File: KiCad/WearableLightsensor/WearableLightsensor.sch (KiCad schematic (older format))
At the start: 2 parts

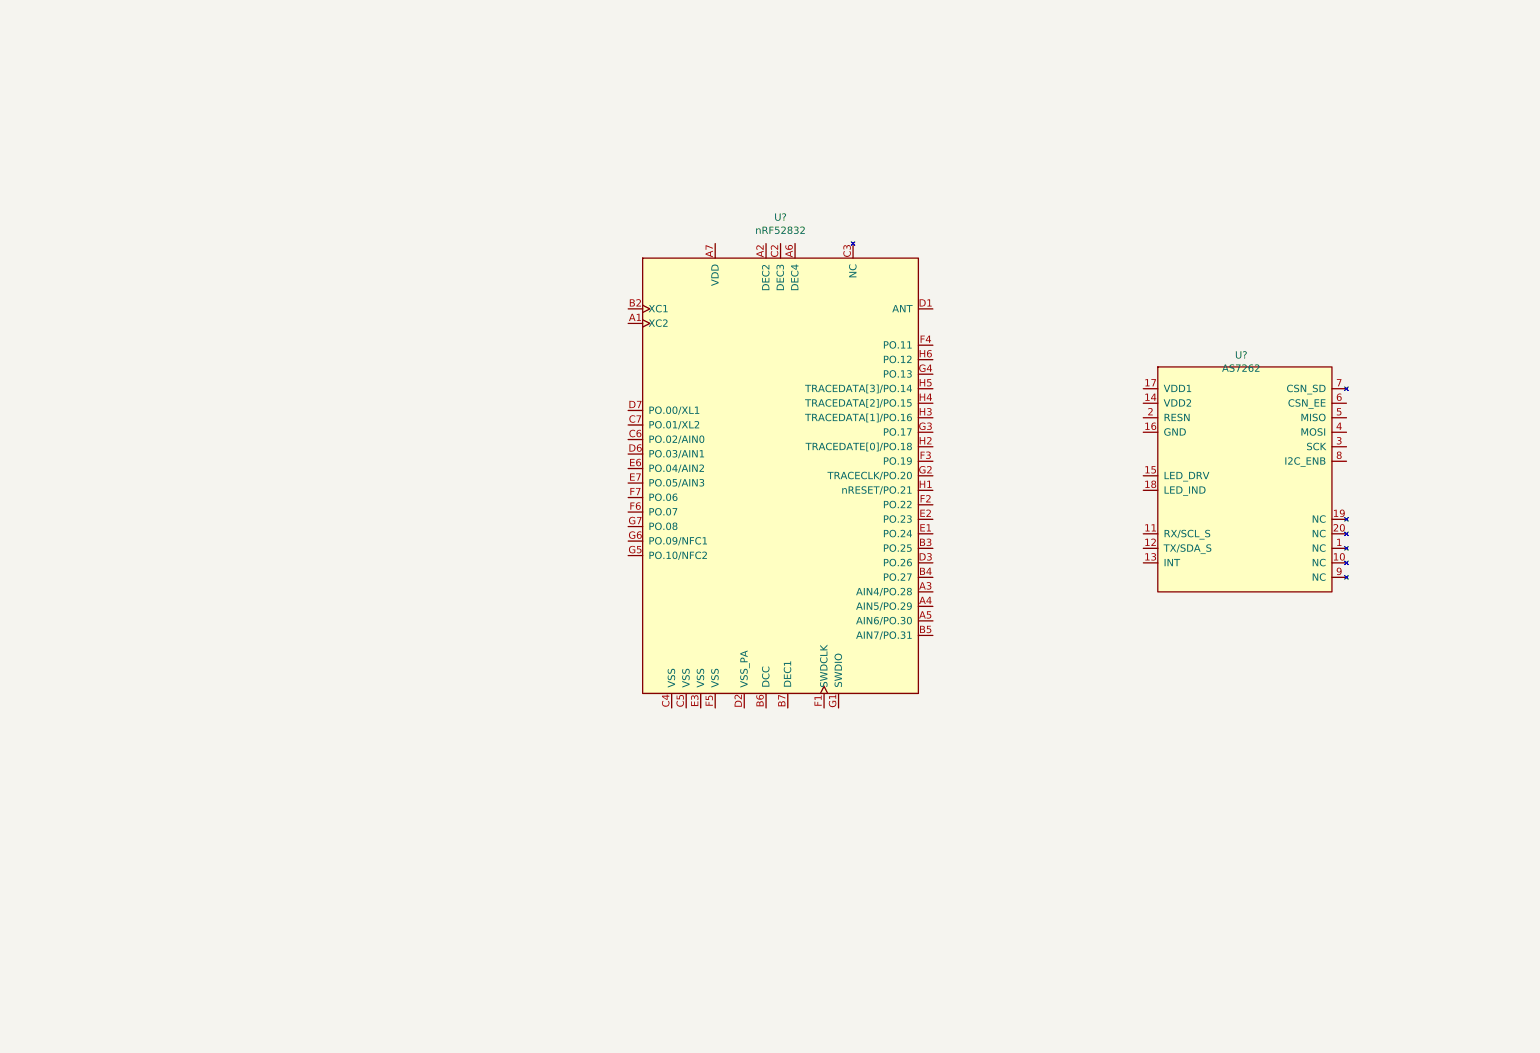
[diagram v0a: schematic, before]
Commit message: Finalize schematic. Begin work on layout
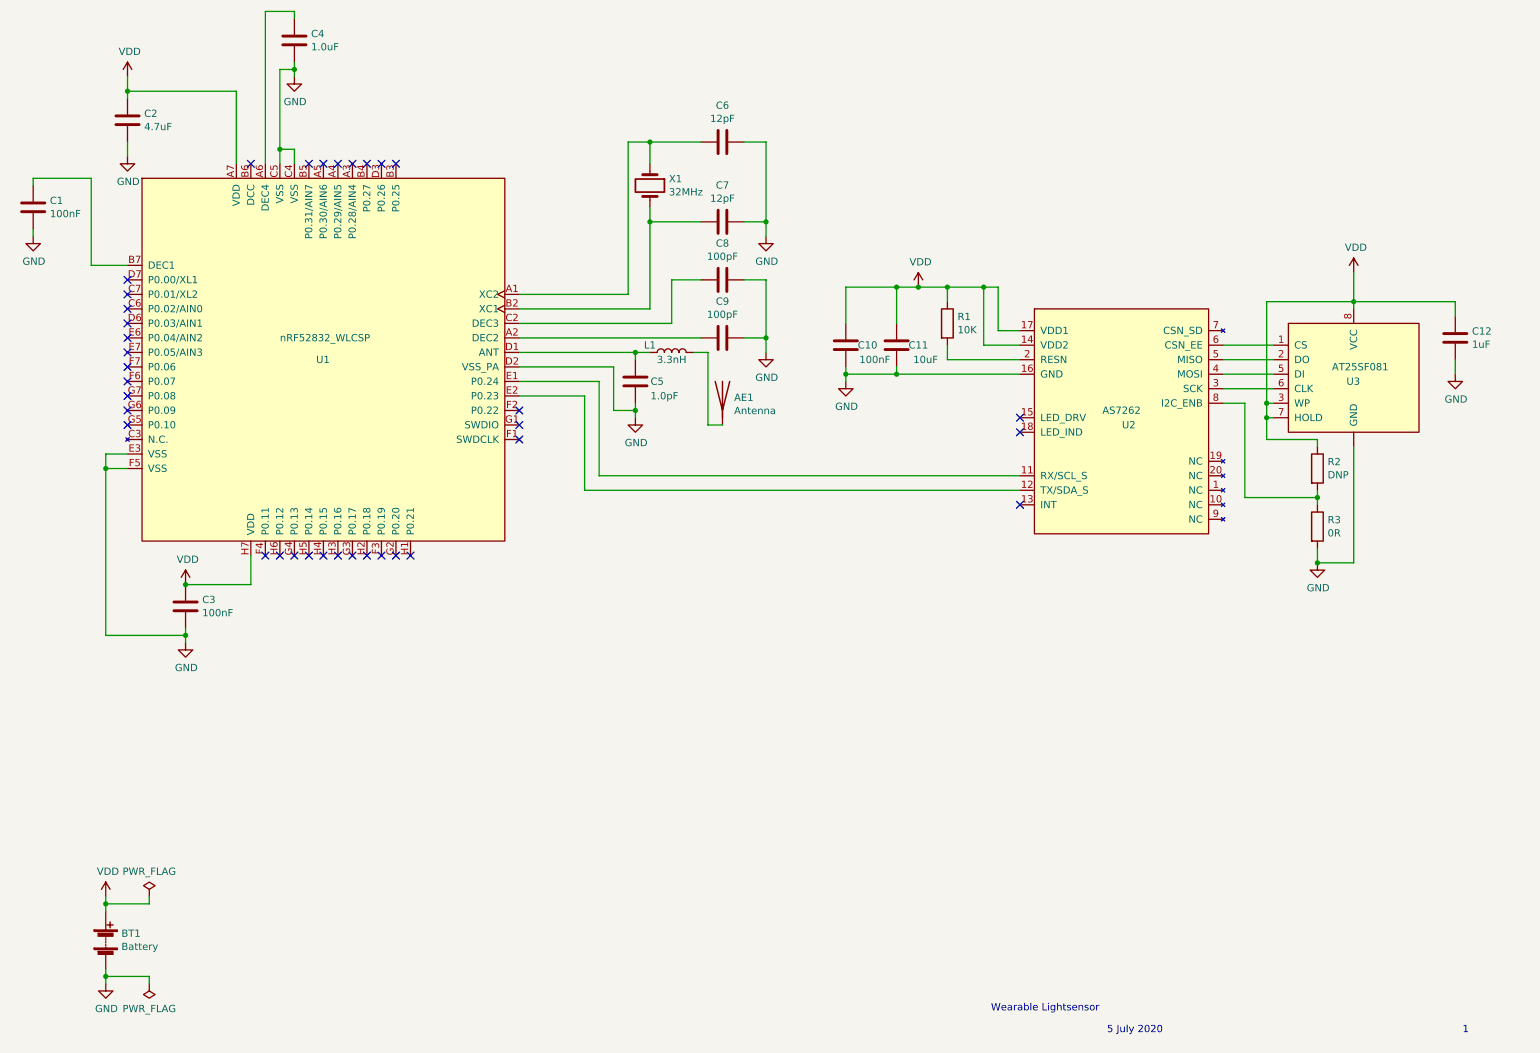
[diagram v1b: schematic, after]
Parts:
- removed U?: nRF52832, symbol WearableLightsensor:nRF52832
- removed U?: AS7262, symbol WearableLightsensor:AS7262
- added AE1: Antenna, RF_Antenna:Texas_SWRA117D_2.4GHz_Left, symbol Device:Antenna
- added BT1: Battery, Battery:BatteryHolder_MPD_BC2003_1x2032, symbol Device:Battery
- added C1, C10, C3: 100nF, Capacitor_SMD:C_0201_0603Metric, symbol Device:C
- added C11: 10uF, Capacitor_SMD:C_0603_1608Metric, symbol Device:C
- added C12: 1uF, Capacitor_SMD:C_0402_1005Metric, symbol Device:C
- added C2: 4.7uF, Capacitor_SMD:C_0603_1608Metric, symbol Device:C
- added C4: 1.0uF, Capacitor_SMD:C_0402_1005Metric, symbol Device:C
- added C5: 1.0pF, Capacitor_SMD:C_0201_0603Metric, symbol Device:C
- added C6, C7: 12pF, Capacitor_SMD:C_0201_0603Metric, symbol Device:C
- added C8, C9: 100pF, Capacitor_SMD:C_0201_0603Metric, symbol Device:C
- added L1: 3.3nH, Inductor_SMD:L_0201_0603Metric, symbol Device:L
- added R1: 10K, Capacitor_SMD:C_0402_1005Metric, symbol Device:R
- added R2: DNP, Capacitor_SMD:C_0402_1005Metric, symbol Device:R
- added R3: 0R, Capacitor_SMD:C_0402_1005Metric, symbol Device:R
- added U1: nRF52832_WLCSP, FootprintLib:BGA-56_7x8_2.956x3.226mm, symbol WearableLightsensor:nRF52832_WLCSP
- added U2: AS7262, Package_LGA:AMS_LGA-20_4.7x4.5mm_P0.65mm, symbol WearableLightsensor:AS7262
- added U3: AT25SF081, Package_SO:SOIC-8_3.9x4.9mm_P1.27mm, symbol WearableLightsensor:AT25SF081
- added X1: 32MHz, Crystal:Crystal_SMD_2016-4Pin_2.0x1.6mm, symbol Device:Crystal
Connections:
- new net: C6.2, U1.A1 (XC2), X1.1
- new net: C9.2, U1.A2 (DEC2)
- new net: C4.1, U1.A6 (DEC4)
- new net: C7.2, U1.B2 (XC1), X1.2
- new net: C1.1, U1.B7 (DEC1)
- new net: C8.2, U1.C2 (DEC3)
- new net: C5.2, L1.1, U1.D1 (ANT)
- new net: U1.E1 (P0.24), U2.11 (RX/SCL_S)
- new net: U1.E2 (P0.23), U2.12 (TX/SDA_S)
- new net: AE1.1 (A), L1.2
- new net: R1.2, U2.2 (RESN)
- new net: U2.3 (SCK), U3.6 (CLK)
- new net: U2.4 (MOSI), U3.5 (DI)
- new net: U2.5 (MISO), U3.2 (DO)
- new net: U2.6 (CSN_EE), U3.1 (CS)
- new net: R2.2, R3.1, U2.8 (I2C_ENB)
- new net GND: BT1.2 (-), C1.2, C10.1, C11.1, C12.2, C2.2, C3.2, C4.2, C5.1, C6.1, C7.1, C8.1, C9.1, R3.2, U1.C4 (VSS), U1.C5 (VSS), U1.D2 (VSS_PA), U1.E3 (VSS), U1.F5 (VSS), U2.16 (GND), U3.~ (GND)
- new net VDD: BT1.1 (+), C10.2, C11.2, C12.1, C2.1, C3.1, R1.1, R2.1, U1.A7 (VDD), U1.H7 (VDD), U2.14 (VDD2), U2.17 (VDD1), U3.3 (WP), U3.7 (HOLD), U3.8 (VCC)
- no-connect marks 0 -> 36
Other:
- note added: "1"
- note added: "5 July 2020"
- note added: "Wearable Lightsensor"

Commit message: Revert to QFN package. There is enough room
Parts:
- removed AE1: Antenna, RF_Antenna:Texas_SWRA117D_2.4GHz_Left, symbol Device:Antenna
- removed C1, C3: 100nF, Capacitor_SMD:C_0201_0603Metric, symbol Device:C
- removed C2: 4.7uF, Capacitor_SMD:C_0603_1608Metric, symbol Device:C
- removed C4: 1.0uF, Capacitor_SMD:C_0402_1005Metric, symbol Device:C
- removed C5: 1.0pF, Capacitor_SMD:C_0201_0603Metric, symbol Device:C
- removed C6, C7: 12pF, Capacitor_SMD:C_0201_0603Metric, symbol Device:C
- removed C8, C9: 100pF, Capacitor_SMD:C_0201_0603Metric, symbol Device:C
- removed L1: 3.3nH, Inductor_SMD:L_0201_0603Metric, symbol Device:L
- removed U1: nRF52832_WLCSP, FootprintLib:BGA-56_7x8_2.956x3.226mm, symbol WearableLightsensor:nRF52832_WLCSP
- removed X1: 32MHz, Crystal:Crystal_SMD_2016-4Pin_2.0x1.6mm, symbol Device:Crystal
- added AE?: Antenna, RF_Antenna:Texas_SWRA117D_2.4GHz_Left, symbol Device:Antenna
- added C? (x2): 12pF, Capacitor_SMD:C_0402_1005Metric, symbol Device:C
- added C?: 100pF, Capacitor_SMD:C_0402_1005Metric, symbol Device:C
- added C?: N.C., Capacitor_SMD:C_0402_1005Metric, symbol Device:C
- added C?: 0.8pF, Capacitor_SMD:C_0402_1005Metric, symbol Device:C
- added C? (x3): 100nF, Capacitor_SMD:C_0402_1005Metric, symbol Device:C
- added C?: 4.7uF, Capacitor_SMD:C_0603_1608Metric, symbol Device:C
- added C?: 1.0uF, Capacitor_SMD:C_0603_1608Metric, symbol Device:C
- added L?: 3.9nH, Inductor_SMD:L_0402_1005Metric, symbol Device:L
- added U?: nRF52832_QFN, symbol WearableLightsensor:nRF52832_QFN
- added X?: 32MHz, Crystal:Crystal_SMD_2016-4Pin_2.0x1.6mm, symbol Device:Crystal
- U3: symbol WearableLightsensor:AT25SF081 -> WearableLightsensor-rescue:AT25SF081-WearableLightsensor
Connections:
- net labels added: SCL, SDA
- no-connect marks 36 -> 3
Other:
- note added: "MICROCONTROLLER"
- note added: "POWER\n"
- note added: "SENSOR"
- moved on the sheet: BT1, C10, C11, C12, R1, R2, R3, U2

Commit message: Fix uP symbol and make schematic pass ERC
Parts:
- U1: renamed from U?; footprint (none) -> Package_DFN_QFN:QFN-48-1EP_6x6mm_P0.4mm_EP4.6x4.6mm
- gave numbers to parts that had none: 13
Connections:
- no-connect marks 3 -> 37
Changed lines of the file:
@@
 5 July 2020
 $Comp
-L WearableLightsensor:nRF52832_QFN U?
+L WearableLightsensor:nRF52832_QFN U1
 U 1 1 5F301DDC
 P 2750 5800
-F 0 "U?" H 2750 5900 50  0000 L CNN
+F 0 "U1" H 2750 5900 50  0000 L CNN
 F 1 "nRF52832_QFN" H 2500 6000 50  0000 L CNN
-F 2 "" H 2750 5800 50  0001 C CNN
+F 2 "Package_DFN_QFN:QFN-48-1EP_6x6mm_P0.4mm_EP4.6x4.6mm" H 2750 5800 50  0001 C CNN
 F 3 "" H 2750 5800 50  0001 C CNN
 	1    2750 5800
@@
 $EndComp
 $Comp
-L Device:Crystal X?
+L Device:Crystal X1
 U 1 1 5F311D90
 P 4900 4000
-F 0 "X?" V 4854 4131 50  0000 L CNN
+F 0 "X1" V 4854 4131 50  0000 L CNN
 F 1 "32MHz" V 4945 4131 50  0000 L CNN
 F 2 "Crystal:Crystal_SMD_2016-4Pin_2.0x1.6mm" H 4900 4000 50  0001 C CNN
@@
 $EndComp
 $Comp
-L Device:C C?
+L Device:C C8
 U 1 1 5F313B1A
 P 5400 4200
-F 0 "C?" V 5148 4200 50  0000 C CNN
+F 0 "C8" V 5148 4200 50  0000 C CNN
 F 1 "12pF" V 5239 4200 50  0000 C CNN
 F 2 "Capacitor_SMD:C_0402_1005Metric" H 5438 4050 50  0001 C CNN
@@
 $EndComp
 $Comp
-L Device:C C?
+L Device:C C7
 U 1 1 5F314DA8
 P 5400 3800
-F 0 "C?" V 5148 3800 50  0000 C CNN
+F 0 "C7" V 5148 3800 50  0000 C CNN
 F 1 "12pF" V 5239 3800 50  0000 C CNN
 F 2 "Capacitor_SMD:C_0402_1005Metric" H 5438 3650 50  0001 C CNN
@@
 $EndComp
 $Comp
-L power:GND #PWR?
+L power:GND #PWR017
 U 1 1 5F31610B
 P 5700 4400
-F 0 "#PWR?" H 5700 4150 50  0001 C CNN
+F 0 "#PWR017" H 5700 4150 50  0001 C CNN
 F 1 "GND" H 5705 4227 50  0000 C CNN
 F 2 "" H 5700 4400 50  0001 C CNN
@@
 Connection ~ 4900 4200
 $Comp
-L Device:C C?
+L Device:C C9
 U 1 1 5F320F0A
 P 5400 4700
-F 0 "C?" V 5148 4700 50  0000 C CNN
+F 0 "C9" V 5148 4700 50  0000 C CNN
 F 1 "100pF" V 5239 4700 50  0000 C CNN
 F 2 "Capacitor_SMD:C_0402_1005Metric" H 5438 4550 50  0001 C CNN
@@
 $EndComp
 $Comp
-L Device:C C?
+L Device:C C13
 U 1 1 5F3235BB
 P 5400 5100
-F 0 "C?" V 5148 5100 50  0000 C CNN
+F 0 "C13" V 5148 5100 50  0000 C CNN
 F 1 "N.C." V 5239 5100 50  0000 C CNN
 F 2 "Capacitor_SMD:C_0402_1005Metric" H 5438 4950 50  0001 C CNN
@@
 $EndComp
 $Comp
-L power:GND #PWR?
+L power:GND #PWR018
 U 1 1 5F323C18
 P 5700 5200
-F 0 "#PWR?" H 5700 4950 50  0001 C CNN
+F 0 "#PWR018" H 5700 4950 50  0001 C CNN
 F 1 "GND" H 5705 5027 50  0000 C CNN
 F 2 "" H 5700 5200 50  0001 C CNN
@@
 	5550 5100 5700 5100
 $Comp
-L Device:C C?
+L Device:C C6
 U 1 1 5F340153
 P 5250 6000
-F 0 "C?" H 5365 6046 50  0000 L CNN
+F 0 "C6" H 5365 6046 50  0000 L CNN
 F 1 "0.8pF" H 5365 5955 50  0000 L CNN
 F 2 "Capacitor_SMD:C_0402_1005Metric" H 5288 5850 50  0001 C CNN
@@
 $EndComp
 $Comp
-L Device:L L?
+L Device:L L1
 U 1 1 5F34142D
 P 5500 5750
-F 0 "L?" V 5690 5750 50  0000 C CNN
+F 0 "L1" V 5690 5750 50  0000 C CNN
 F 1 "3.9nH" V 5599 5750 50  0000 C CNN
 F 2 "Inductor_SMD:L_0402_1005Metric" H 5500 5750 50  0001 C CNN
@@
 	5250 6200 5250 6150
 $Comp
-L power:GND #PWR?
+L power:GND #PWR09
 U 1 1 5F3671BD
 P 5250 6250
-F 0 "#PWR?" H 5250 6000 50  0001 C CNN
+F 0 "#PWR09" H 5250 6000 50  0001 C CNN
 F 1 "GND" H 5255 6077 50  0000 C CNN
 F 2 "" H 5250 6250 50  0001 C CNN
@@
 	5250 5750 5350 5750
 $Comp
-L Device:Antenna AE?
+L Device:Antenna AE1
 U 1 1 5F36C552
 P 6050 5500
-F 0 "AE?" H 6130 5489 50  0000 L CNN
+F 0 "AE1" H 6130 5489 50  0000 L CNN
 F 1 "Antenna" H 6130 5398 50  0000 L CNN
 F 2 "RF_Antenna:Texas_SWRA117D_2.4GHz_Left" H 6050 5500 50  0001 C CNN
@@
 	6050 5750 6050 5700
 $Comp
-L power:VDD #PWR?
+L power:VDD #PWR07
 U 1 1 5F370122
 P 4400 4500
-F 0 "#PWR?" H 4400 4350 50  0001 C CNN
+F 0 "#PWR07" H 4400 4350 50  0001 C CNN
 F 1 "VDD" H 4415 4673 50  0000 C CNN
 F 2 "" H 4400 4500 50  0001 C CNN
@@
 $EndComp
 $Comp
-L Device:C C?
+L Device:C C5
 U 1 1 5F3714B3
 P 4400 4750
-F 0 "C?" H 4285 4704 50  0000 R CNN
+F 0 "C5" H 4285 4704 50  0000 R CNN
 F 1 "100nF" H 4285 4795 50  0000 R CNN
 F 2 "Capacitor_SMD:C_0402_1005Metric" H 4438 4600 50  0001 C CNN
@@
 $EndComp
 $Comp
-L power:GND #PWR?
+L power:GND #PWR08
 U 1 1 5F3730AC
 P 4400 5000
-F 0 "#PWR?" H 4400 4750 50  0001 C CNN
+F 0 "#PWR08" H 4400 4750 50  0001 C CNN
 F 1 "GND" H 4405 4827 50  0000 C CNN
 F 2 "" H 4400 5000 50  0001 C CNN
@@
 	4400 4550 4400 4600
 $Comp
-L power:VDD #PWR?
+L power:VDD #PWR02
 U 1 1 5F397B77
 P 950 6900
-F 0 "#PWR?" H 950 6750 50  0001 C CNN
+F 0 "#PWR02" H 950 6750 50  0001 C CNN
 F 1 "VDD" H 965 7073 50  0000 C CNN
 F 2 "" H 950 6900 50  0001 C CNN
@@
 $EndComp
 $Comp
-L Device:C C?
+L Device:C C2
 U 1 1 5F39BE02
 P 950 7150
-F 0 "C?" H 835 7104 50  0000 R CNN
+F 0 "C2" H 835 7104 50  0000 R CNN
 F 1 "100nF" H 835 7195 50  0000 R CNN
 F 2 "Capacitor_SMD:C_0402_1005Metric" H 988 7000 50  0001 C CNN
@@
 $EndComp
 $Comp
-L power:GND #PWR?
+L power:GND #PWR03
 U 1 1 5F39C80B
 P 950 7400
-F 0 "#PWR?" H 950 7150 50  0001 C CNN
+F 0 "#PWR03" H 950 7150 50  0001 C CNN
 F 1 "GND" H 955 7227 50  0000 C CNN
 F 2 "" H 950 7400 50  0001 C CNN
@@
 	950  7300 950  7400
 $Comp
-L Device:C C?
+L Device:C C1
 U 1 1 5F3A6675
 P 850 4650
-F 0 "C?" H 735 4604 50  0000 R CNN
+F 0 "C1" H 735 4604 50  0000 R CNN
 F 1 "100nF" H 735 4695 50  0000 R CNN
 F 2 "Capacitor_SMD:C_0402_1005Metric" H 888 4500 50  0001 C CNN
@@
 $EndComp
 $Comp
-L power:GND #PWR?
+L power:GND #PWR01
 U 1 1 5F3A6DAE
 P 850 4900
-F 0 "#PWR?" H 850 4650 50  0001 C CNN
+F 0 "#PWR01" H 850 4650 50  0001 C CNN
 F 1 "GND" H 855 4727 50  0000 C CNN
 F 2 "" H 850 4900 50  0001 C CNN
@@
 	850  4400 850  4500
 $Comp
-L Device:C C?
+L Device:C C3
 U 1 1 5F3B31A9
 P 1750 4000
-F 0 "C?" H 1635 3954 50  0000 R CNN
+F 0 "C3" H 1635 3954 50  0000 R CNN
 F 1 "4.7uF" H 1635 4045 50  0000 R CNN
 F 2 "Capacitor_SMD:C_0603_1608Metric" H 1788 3850 50  0001 C CNN
@@
 $EndComp
 $Comp
-L power:GND #PWR?
+L power:GND #PWR05
 U 1 1 5F3B375C
 P 1750 4250
-F 0 "#PWR?" H 1750 4000 50  0001 C CNN
+F 0 "#PWR05" H 1750 4000 50  0001 C CNN
 F 1 "GND" H 1755 4077 50  0000 C CNN
 F 2 "" H 1750 4250 50  0001 C CNN
@@
 $EndComp
 $Comp
-L power:VDD #PWR?
+L power:VDD #PWR04
 U 1 1 5F3B3DD7
 P 1750 3750
-F 0 "#PWR?" H 1750 3600 50  0001 C CNN
+F 0 "#PWR04" H 1750 3600 50  0001 C CNN
 F 1 "VDD" H 1765 3923 50  0000 C CNN
 F 2 "" H 1750 3750 50  0001 C CNN
@@
 	1750 4150 1750 4250
 $Comp
-L Device:C C?
+L Device:C C4
 U 1 1 5F3BF755
 P 2600 3700
-F 0 "C?" H 2485 3654 50  0000 R CNN
+F 0 "C4" H 2485 3654 50  0000 R CNN
 F 1 "1.0uF" H 2485 3745 50  0000 R CNN
 F 2 "Capacitor_SMD:C_0603_1608Metric" H 2638 3550 50  0001 C CNN
@@
 $EndComp
 $Comp
-L power:GND #PWR?
+L power:GND #PWR06
 U 1 1 5F3BFE8B
 P 2600 4000
-F 0 "#PWR?" H 2600 3750 50  0001 C CNN
+F 0 "#PWR06" H 2600 3750 50  0001 C CNN
 F 1 "GND" H 2605 3827 50  0000 C CNN
 F 2 "" H 2600 4000 50  0001 C CNN
@@
 Text Notes 6100 3250 0    50   ~ 0
 SENSOR
+NoConn ~ 1400 5350
+NoConn ~ 1400 5450
+NoConn ~ 1400 5550
+NoConn ~ 1400 5650
+NoConn ~ 1400 5750
+NoConn ~ 1400 5850
+NoConn ~ 1400 5950
+NoConn ~ 1400 6050
+NoConn ~ 1400 6150
+NoConn ~ 1400 6250
+NoConn ~ 1400 6350
+NoConn ~ 2300 7100
+NoConn ~ 2400 7100
+NoConn ~ 2500 7100
+NoConn ~ 2600 7100
+NoConn ~ 2700 7100
+NoConn ~ 2800 7100
+NoConn ~ 2900 7100
+NoConn ~ 3000 7100
+NoConn ~ 3100 7100
+NoConn ~ 3200 7100
+NoConn ~ 3300 7100
+NoConn ~ 4100 6150
+NoConn ~ 4100 6250
+NoConn ~ 4100 6350
+NoConn ~ 2300 4400
+NoConn ~ 2600 4400
+NoConn ~ 2700 4400
+NoConn ~ 2800 4400
+NoConn ~ 2900 4400
+NoConn ~ 3000 4400
+NoConn ~ 3100 4400
+NoConn ~ 3200 4400
+NoConn ~ 3300 4400
 $EndSCHEMATC
